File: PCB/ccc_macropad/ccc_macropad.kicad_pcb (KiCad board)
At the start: 2 copper layers, 101.5 x 44 mm, 18 parts, among them SW1 SW_Push, SW2 SW_Push, SW3 OS/Left_Right-hand_Switch, SW4 SW_Push, SW5 SW_Push, U2 XIAO-RP2040-DIP

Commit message: fix: footprint switch / add ground plane front
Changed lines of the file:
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@@
 		(13 "F.Paste" user)
 		(15 "B.Paste" user)
-		(5 "F.SilkS" user)
-		(7 "B.SilkS" user)
+		(5 "F.SilkS" user "F.Silkscreen")
+		(7 "B.SilkS" user "B.Silkscreen")
 		(1 "F.Mask" user)
 		(3 "B.Mask" user)
 		(25 "Edge.Cuts" user)
 		(27 "Margin" user)
-		(31 "F.CrtYd" user)
-		(29 "B.CrtYd" user)
+		(31 "F.CrtYd" user "F.Courtyard")
+		(29 "B.CrtYd" user "B.Courtyard")
 		(35 "F.Fab" user)
 	)
@@
 			(outputformat 1)
 			(mirror no)
-			(drillshape 1)
+			(drillshape 0)
 			(scaleselection 1)
-			(outputdirectory "")
+			(outputdirectory "gerbers/")
 		)
 	)
@@
 	(net 18 "Net-(U2-GPIO2{slash}SCK)")
 	(net 19 "Net-(U2-GPIO4{slash}MISO)")
-	(net 20 "unconnected-(U2-GPIO7{slash}SCL-Pad6)")
-	(net 21 "unconnected-(U2-GPIO6{slash}SDA-Pad5)")
-	(net 22 "unconnected-(U2-GPIO7{slash}SCL-Pad6)_1")
-	(net 23 "unconnected-(U2-GPIO6{slash}SDA-Pad5)_1")
-	(net 24 "unconnected-(U2-VBUS-Pad14)")
-	(net 25 "unconnected-(U2-VBUS-Pad14)_1")
+	(net 20 "unconnected-(U2-GPIO7{slash}SCL-Pad6)_1")
+	(net 21 "unconnected-(U2-GPIO6{slash}SDA-Pad5)_1")
+	(net 22 "unconnected-(U2-VBUS-Pad14)")
 	(footprint "LED_THT:LED_D3.0mm"
 		(layer "F.Cu")
@@
 			(layers "F.Cu" "F.Mask")
 			(roundrect_rratio 0.1)
-			(net 23 "unconnected-(U2-GPIO6{slash}SDA-Pad5)_1")
+			(net 21 "unconnected-(U2-GPIO6{slash}SDA-Pad5)_1")
 			(pinfunction "GPIO6/SDA")
 			(pintype "passive+no_connect")
@@
 			(layers "*.Cu" "*.Mask")
 			(remove_unused_layers no)
-			(net 21 "unconnected-(U2-GPIO6{slash}SDA-Pad5)")
+			(net 21 "unconnected-(U2-GPIO6{slash}SDA-Pad5)_1")
 			(pinfunction "GPIO6/SDA")
 			(pintype "passive+no_connect")
@@
 			(layers "F.Cu" "F.Mask")
 			(roundrect_rratio 0.1)
-			(net 22 "unconnected-(U2-GPIO7{slash}SCL-Pad6)_1")
+			(net 20 "unconnected-(U2-GPIO7{slash}SCL-Pad6)_1")
 			(pinfunction "GPIO7/SCL")
 			(pintype "passive+no_connect")
@@
 			(layers "*.Cu" "*.Mask")
 			(remove_unused_layers no)
-			(net 20 "unconnected-(U2-GPIO7{slash}SCL-Pad6)")
+			(net 20 "unconnected-(U2-GPIO7{slash}SCL-Pad6)_1")
 			(pinfunction "GPIO7/SCL")
 			(pintype "passive+no_connect")
@@
 			(layers "*.Cu" "*.Mask")
 			(remove_unused_layers no)
-			(net 24 "unconnected-(U2-VBUS-Pad14)")
+			(net 22 "unconnected-(U2-VBUS-Pad14)")
 			(pinfunction "VBUS")
 			(pintype "passive+no_connect")
@@
 			(layers "F.Cu" "F.Mask")
 			(roundrect_rratio 0.1)
-			(net 25 "unconnected-(U2-VBUS-Pad14)_1")
+			(net 22 "unconnected-(U2-VBUS-Pad14)")
 			(pinfunction "VBUS")
 			(pintype "passive+no_connect")
@@
 			(layer "F.Fab")
 		)
+		(fp_text user "K"
+			(at 0 -1.8 90)
+			(layer "Cmts.User")
+			(effects
+				(font
+					(size 1 1)
+					(thickness 0.15)
+				)
+			)
+		)
 		(fp_text user "${REFERENCE}"
 			(at 4.0875 0 90)
@@
 		(sheetfile "ccc_macropad.kicad_sch")
 		(attr through_hole)
-		(fp_rect
+		(fp_line
 			(start 0 0)
+			(end 0 1)
+			(stroke
+				(width 0.1)
+				(type default)
+			)
+			(layer "F.SilkS")
+		)
+		(fp_line
+			(start 0 0)
+			(end 8.6 0)
+			(stroke
+				(width 0.1)
+				(type default)
+			)
+			(layer "F.SilkS")
+		)
+		(fp_line
+			(start 0 4.5)
+			(end 0 3.5)
+			(stroke
+				(width 0.1)
+				(type default)
+			)
+			(layer "F.SilkS")
+		)
+		(fp_line
+			(start 0 4.5)
 			(end 8.6 4.5)
 			(stroke
 				(width 0.1)
-				(type solid)
+				(type default)
+			)
+			(layer "F.SilkS")
+		)
+		(fp_line
+			(start 8.6 0)
+			(end 8.6 1)
+			(stroke
+				(width 0.1)
+				(type default)
+			)
+			(layer "F.SilkS")
+		)
+		(fp_line
+			(start 8.6 4.5)
+			(end 8.6 3.5)
+			(stroke
+				(width 0.1)
+				(type default)
 			)
-			(fill no)
 			(layer "F.SilkS")
 		)

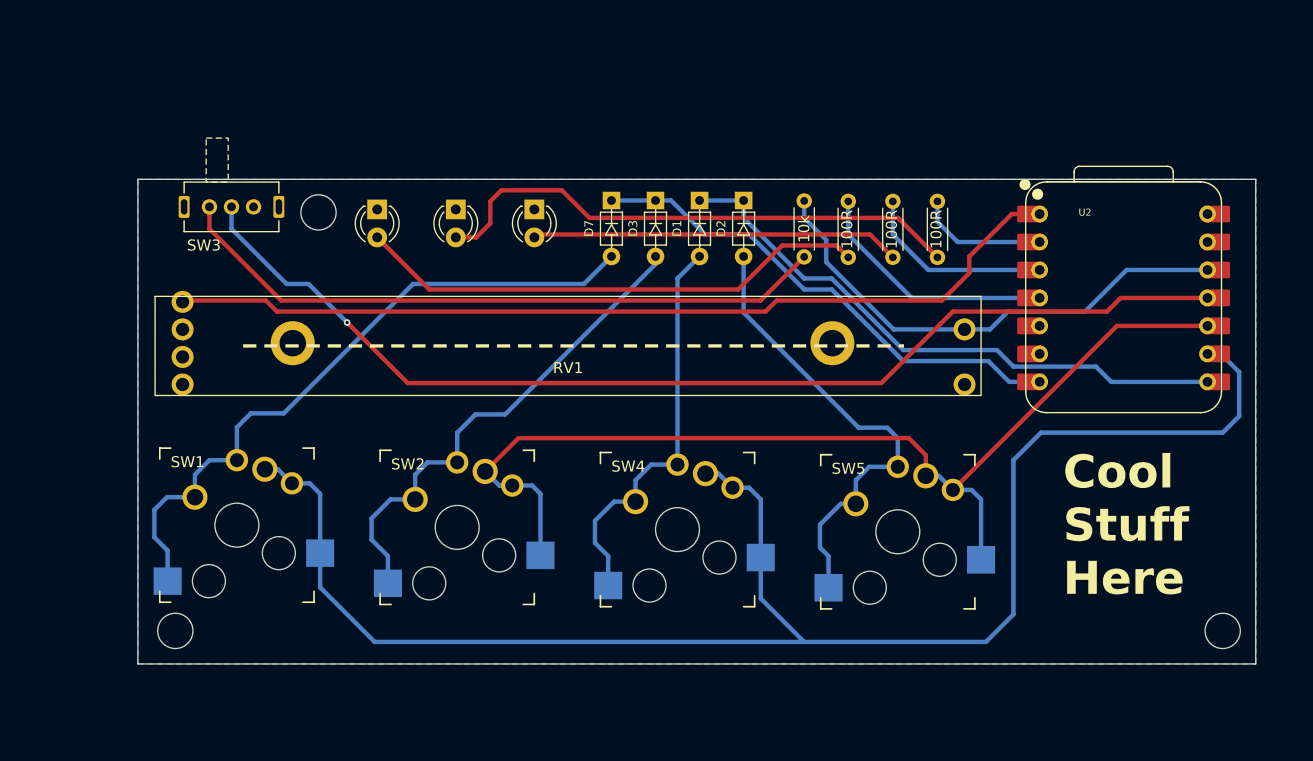
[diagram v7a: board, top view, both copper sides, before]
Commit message: rm font / add front ground plane
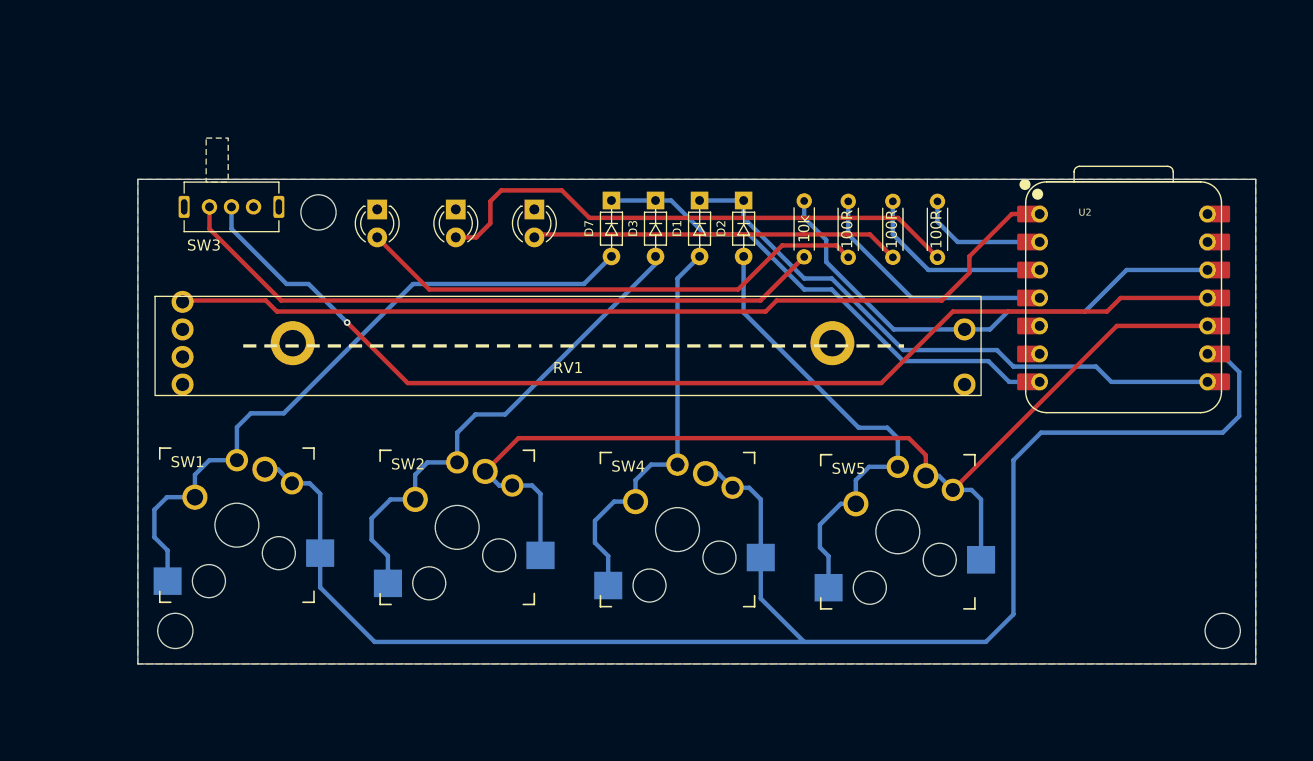
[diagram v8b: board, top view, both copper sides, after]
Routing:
- added copper zone on F.Cu, net GND
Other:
- board text removed: "Cool Stuff Here"
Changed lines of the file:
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@@
 		(layer "Edge.Cuts")
-	)
-	(gr_text "Cool\nStuff\nHere"
-		(at 194.5 76 0)
-		(layer "F.SilkS")
-		(effects
-			(font
-				(size 3 3)
-				(thickness 0.75)
-				(bold yes)
-			)
-			(justify left bottom)
-		)
 	)
 	(gr_text "-"
@@
 	)
 	(zone
+		(net 8)
+		(net_name "GND")
+		(layer "F.Cu")
+		(hatch edge 0.5)
+		(priority 1)
+		(connect_pads
+			(clearance 0.5)
+		)
+		(min_thickness 0.25)
+		(filled_areas_thickness no)
+		(fill yes
+			(thermal_gap 0.5)
+			(thermal_bridge_width 0.5)
+		)
+		(polygon
+			(pts
+				(xy 110.5 38) (xy 212 38) (xy 212 82) (xy 110.5 82)
+			)
+		)
+	)
+	(zone
